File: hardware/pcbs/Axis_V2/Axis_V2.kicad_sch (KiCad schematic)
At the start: 12 parts, among them SW2 RES, U1 ADS1119IPWR, U2 MAX6107, U3 Pico, U5 TCA9534, U9 TCA9548APWR

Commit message: Updates
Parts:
- removed U9: TCA9548APWR, Package_SO:TSSOP-24_4.4x7.8mm_P0.65mm, symbol Interface_Expansion:TCA9548APWR
- added C3: 100n, symbol Device:C_Small
- added J1: Conn_01x12, symbol Connector_Generic:Conn_01x12
- added J12: Conn_01x08, symbol Connector_Generic:Conn_01x08
- added J13: UART, symbol Connector_Generic:Conn_01x03
- added J14: SWD, symbol Connector_Generic:Conn_01x03
- added J4: Conn_01x06, symbol Connector_Generic:Conn_01x06
- added J5: Conn_01x10, Connector_IDC:IDC-Header_2x10_P2.54mm_Vertical, symbol Connector_Generic:Conn_01x10
- added J6: Conn_01x07, symbol Connector_Generic:Conn_01x07
- added J8, J9: Conn_01x03, symbol Connector_Generic:Conn_01x03
- added JP1: EEPROM_WP, Jumper:SolderJumper-3_P2.0mm_Open_TrianglePad1.0x1.5mm, symbol Jumper:SolderJumper_3_Open
- added R15, R16, R17, R18, R19, R20, R21, R22, R23, R24, R25, R26, R3, R4, R5, R6: 1k, symbol Device:R_Small
- added TP1, TP10, TP11, TP12, TP13, TP16, TP17, TP18, TP19, TP4, TP5, TP6, TP7, TP8, TP9: ~, TestPoint:TestPoint_Pad_1.5x1.5mm, symbol Connector:TestPoint
- added U3: FM24CL16B, Package_SO:SOIC-8_3.9x4.9mm_P1.27mm, symbol Memory_NVRAM:FM24CL16B
- added U5: TCA9544A, Package_SO:TSSOP-20_4.4x6.5mm_P0.65mm, symbol Interface_Expansion:TCA9544A
- added U6: 74HC138, symbol 74xx:74HC138
- renumbered C3 to C4, C4 to C5, SW2 to SW1, U5 to U1, U3 to U2, U1 to U4, U2 to U7
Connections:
- net SPI1_CS2 is gone; now on net SPI1_TX: U2.15 (GPIO11)
- net +3V3: now also C3.1, J12.1 (Pin_1), J4.1 (Pin_1), J5.1 (Pin_1), J6.1 (Pin_1), J6.7 (Pin_7), JP1.1 (A), R15.1, R16.1, R17.1, R18.1, R19.1, R20.1, R21.1, R22.1, R23.1, R24.1, R25.1, R26.1, R3.1, R4.1, R5.1, R6.1, U3.8 (VDD), U5.20 (VCC), U6.16 (VCC)
- net +5V: now also J8.1 (Pin_1), J9.1 (Pin_1)
- net 4.5V_VREF: now also TP12.1
- net GND: now also C3.2, J12.8 (Pin_8), J13.2 (Pin_2), J14.2 (Pin_2), J5.2 (Pin_2), J6.2 (Pin_2), J8.3 (Pin_3), J9.3 (Pin_3), JP1.3 (B), U3.4 (VSS), U5.1 (A0), U5.10 (GND), U5.2 (A1), U5.3 (A2), U6.4 (~{E0}), U6.5 (~{E1}), U6.8 (GND); no longer R1.2, U2.32 (GPIO27_ADC1), U4.14 (~{DRDY})
- net I2C0_SCL: now also R1.2, U1.14 (SCL), U2.12 (GPIO9), U5.18 (SCL); no longer U1.15 (SDA), U2.22 (GPIO17)
- net I2C0_SDA: now also R2.2, U1.15 (SDA), U2.11 (GPIO8), U5.19 (SDA); no longer U1.14 (SCL), U2.21 (GPIO16)
- net I2C1_SCL: now also U2.20 (GPIO15), U3.6 (SCL); no longer U2.12 (GPIO9)
- net I2C1_SDA: now also U2.19 (GPIO14), R5.2, R6.2, U3.5 (SDA); no longer U2.14 (GPIO10)
- net SPI0_CS1: now also U2.9 (GPIO6), U6.1 (A0); no longer U2.17 (GPIO13), U2.27 (GPIO21)
- net SPI0_CS2: now also U2.10 (GPIO7), U6.2 (A1); no longer U2.29 (GPIO22)
- net SPI0_RX: now also U2.6 (GPIO4), J5.7 (Pin_7); no longer U2.26 (GPIO20)
- net SPI0_SCK: now also U2.4 (GPIO2), J5.6 (Pin_6); no longer U2.24 (GPIO18)
- net SPI0_TX: now also U2.5 (GPIO3); no longer U2.25 (GPIO19)
- net SPI1_SCK: now also U2.14 (GPIO10), J6.4 (Pin_4); no longer U2.19 (GPIO14)
- net SPI1_TX: now also J6.3 (Pin_3); no longer U2.20 (GPIO15)
- net SWCLK: now also U2.41 (SWCLK), J14.1 (Pin_1)
- net SWDIO: now also U2.43 (SWDIO), J14.3 (Pin_3)
- net UART_RX: now also J13.1 (Pin_1)
- net UART_TX: now also J13.3 (Pin_3)
- net at U2.33 (AGND): now also TP9.1
- net 3WAY: now reaches U2.34 (GPIO28_ADC2)
- net 3WAY: now also J5.5 (Pin_5), TP7.1
- net at U2.35 (ADC_VREF): now also TP8.1
- net SPI0_CS0: now reaches U2.7 (GPIO5)
- net SPI0_CS0: now also U6.6 (E2)
- net ADC_1: now reaches U4.10 (AIN1)
- net ADC_1: now also J9.2 (Pin_2), TP5.1
- net ADC_0: now reaches U4.11 (AIN0)
- net ADC_0: now also J8.2 (Pin_2), TP4.1
- net ADC_3: now reaches U4.6 (AIN3)
- net ADC_3: now also TP11.1
- net ADC_2: now reaches U4.7 (AIN2)
- net ADC_2: now also TP10.1
- net IO_5: now reaches U1.10 (P5)
- net IO_5: now also J1.9 (Pin_9)
- net IO_6: now reaches U1.11 (P6)
- net IO_6: now also J1.10 (Pin_10)
- net IO_7: now reaches U1.12 (P7)
- net IO_7: now also J1.11 (Pin_11)
- net IO_0: now reaches U1.4 (P0)
- net IO_0: now also J1.2 (Pin_2)
- net IO_1: now reaches U1.5 (P1)
- net IO_1: now also J1.3 (Pin_3)
- net IO_2: now reaches U1.6 (P2)
- net IO_2: now also J1.4 (Pin_4)
- net IO_3: now reaches U1.7 (P3)
- net IO_3: now also J1.5 (Pin_5)
- net IO_4: now reaches U1.9 (P4)
- net IO_4: now also J1.8 (Pin_8)
- net SC0 renamed SCL_0
- net SCL_0: now also R15.2, U5.6 (SC0)
- net SD0 renamed SDA_0
- net SDA_0: now also R16.2, U5.5 (SD0)
- net ~{IOEXP_INT} renamed ZC_SIG
- net ZC_SIG: now also J4.2 (Pin_2), J5.3 (Pin_3), TP1.1; no longer U1.13 (~{INT})
- new net 3v3_{IO}: J1.1 (Pin_1), J1.6 (Pin_6)
- new net DISP_DC: J6.6 (Pin_6), U2.29 (GPIO22)
- new net EEPROM_WP: JP1.2 (C), U3.7 (WP)
- new net GND_{IO}: J1.12 (Pin_12), J1.7 (Pin_7)
- new net GPIO_16: J12.2 (Pin_2), U2.21 (GPIO16)
- new net GPIO_17: J12.3 (Pin_3), U2.22 (GPIO17)
- new net GPIO_18: J12.4 (Pin_4), U2.24 (GPIO18)
- new net GPIO_19: J12.5 (Pin_5), U2.25 (GPIO19)
- new net INT_1: R20.2, U5.7 (~{INT1})
- new net INT_2: R23.2, U5.11 (~{INT2})
- new net INT_3: R26.2, TP13.1, U5.14 (~{INT3})
- new net PUMP: J5.4 (Pin_4), TP6.1, U2.32 (GPIO27_ADC1)
- new net SCL_1: R18.2, U5.9 (SC1)
- new net SCL_2: R21.2, U5.13 (SC2)
- new net SCL_3: R24.2, U5.16 (SC3)
- new net SDA_1: R19.2, U5.8 (SD1)
- new net SDA_2: R22.2, U5.12 (SD2)
- new net SDA_3: R25.2, U5.15 (SD3)
- new net SPI0_CS3: U6.3 (A2)
- new net SPI1_CS0: J6.5 (Pin_5), U2.17 (GPIO13)
- new net ~{CS0}: U6.15 (~{Y0})
- new net ~{CS1}: U6.14 (~{Y1})
- new net ~{CS2}: J5.8 (Pin_8), U6.13 (~{Y2})
- new net ~{CS3}: J5.9 (Pin_9), U6.12 (~{Y3})
- new net ~{CS4}: TP16.1, U6.11 (~{Y4})
- new net ~{CS5}: TP17.1, U6.10 (~{Y5})
- new net ~{CS6}: TP18.1, U6.9 (~{Y6})
- new net ~{CS7}: TP19.1, U6.7 (~{Y7})
- new net ~{I2C_IO_INT}: R3.2, R4.2, U1.13 (~{INT}), U2.26 (GPIO20), U2.27 (GPIO21), U5.17 (~{INT})
- new net ~{INT_0}: R17.2, U4.14 (~{DRDY}), U5.4 (~{INT0})
- no-connect marks 4 -> 2
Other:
- removed sheet Peripherals
- note added: "Adding footprints here for resistors in case we'd want to re-use these pins for other purposes. Gives flexibility if a mistake was made during design."
- note added: "Compatible examples: FM24CL16B - fram (C31082) 24C04 - eeprom (C118280) 24C16 - larger eeprom (C79946) etc..."
- note added: "SPI Chip Select, takes a binary signal on A0-2 and converts it to a single pin to be pulled low. If E2 = Low, all outputs are pulled high. Only using 4 SPI peripherals on SPI0 at the moment. SPI1 is dedicated to display."
- note removed: "I2C Expander."
- moved on the sheet: C1, C2, C4, C5, SW1, U1, U2, U4, U7

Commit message: Updates
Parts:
- removed J1: Conn_01x12, symbol Connector_Generic:Conn_01x12
- removed J12: Conn_01x08, symbol Connector_Generic:Conn_01x08
- removed J4: Conn_01x06, symbol Connector_Generic:Conn_01x06
- removed J5: Conn_01x10, Connector_IDC:IDC-Header_2x10_P2.54mm_Vertical, symbol Connector_Generic:Conn_01x10
- removed J6: Conn_01x07, symbol Connector_Generic:Conn_01x07
- removed R15, R16, R17, R18, R19, R20, R21, R22, R23, R24, R25, R26: 1k, symbol Device:R_Small
- removed TP13, TP16, TP17, TP18, TP19: ~, TestPoint:TestPoint_Pad_1.5x1.5mm, symbol Connector:TestPoint
- removed U5: TCA9544A, Package_SO:TSSOP-20_4.4x6.5mm_P0.65mm, symbol Interface_Expansion:TCA9544A
- removed U6: 74HC138, symbol 74xx:74HC138
- added J1: Conn_01x10, symbol Connector_Generic:Conn_01x10
- added J2, J3: Conn_01x02, symbol Connector_Generic:Conn_01x02
- added J4: Conn_01x08, symbol Connector_Generic:Conn_01x08
- added R7, R8, R9: 1k, symbol Device:R_Small
- added U5, U6: MAX31855EASA, Package_SO:SOIC-8_3.9x4.9mm_P1.27mm, symbol Sensor_Temperature:MAX31855EASA
- U2: footprint RPi_Pico:RPi_Pico_SMD_TH -> MCU_RaspberryPi_and_Boards:RPi_Pico_SMD_TH
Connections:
- net IO_0 is gone; now on net IO_1: U1.4 (P0)
- net SCL_0 is gone; now on net I2C0_SCL: U4.16 (SCL)
- net SDA_0 is gone; now on net I2C0_SDA: U4.15 (SDA)
- net +3V3: now also J1.1 (Pin_1), J4.1 (Pin_1), U5.4 (V_CC), U6.4 (V_CC); no longer R4.1, R5.1, R6.1
- net GND: now also J1.2 (Pin_2), J4.8 (Pin_8), U5.1 (GND), U6.1 (GND)
- net I2C1_SDA: no longer R5.2, R6.2
- net IO_1: now also J1.3 (Pin_3); no longer U1.5 (P1)
- net IO_2: now also U1.5 (P1), J1.4 (Pin_4); no longer U1.6 (P2)
- net IO_3: now also U1.6 (P2), J1.5 (Pin_5); no longer U1.7 (P3)
- net IO_4: now also U1.7 (P3), J1.6 (Pin_6); no longer U1.9 (P4)
- net IO_5: now also U1.9 (P4), J1.7 (Pin_7); no longer U1.10 (P5)
- net IO_6: now also U1.10 (P5), J1.8 (Pin_8); no longer U1.11 (P6)
- net IO_7: now also U1.11 (P6), J1.9 (Pin_9); no longer U1.12 (P7)
- net SPI0_CS0: now also U5.6 (~{CS})
- net SPI0_CS1: now also U6.6 (~{CS})
- net SPI0_RX: now also U5.7 (SO), U6.7 (SO)
- net SPI0_SCK: now also U5.5 (SCK), U6.5 (SCK)
- net ~{I2C_IO_INT}: no longer R4.2, U1.13 (~{INT}), U2.26 (GPIO20), U2.27 (GPIO21)
- net 3WAY: no longer names the net of TP7.1, U2.34 (GPIO28_ADC2)
- net DISP_DC: no longer names the net of U2.29 (GPIO22)
- net GPIO_16 renamed HV_IO1
- net HV_IO1: now also R4.1, R4.2, J4.2 (Pin_2)
- net GPIO_17 renamed HV_IO2
- net HV_IO2: now also R5.1, R5.2, J4.3 (Pin_3)
- net GPIO_18 renamed HV_IO3
- net HV_IO3: now also R6.1, R6.2, J4.4 (Pin_4)
- net GPIO_19 renamed HV_IO4
- net HV_IO4: now also J4.5 (Pin_5), R7.1, R7.2
- net PUMP: no longer names the net of TP6.1, U2.32 (GPIO27_ADC1)
- net SPI0_CS2 renamed ~{I2C0_IO_INT}
- net ~{I2C0_IO_INT}: now also U1.13 (~{INT})
- net ZC_SIG: no longer names the net of TP1.1, U2.31 (GPIO26_ADC0)
- new net HV_IO5: J4.6 (Pin_6), R8.1, R8.2, U2.26 (GPIO20)
- new net HV_IO6: J4.7 (Pin_7), R9.1, R9.2, U2.27 (GPIO21)
- new net IO_8: J1.10 (Pin_10), U1.12 (P7)
- new net THCPL1_NEG: J2.2 (Pin_2), U5.2 (T-)
- new net THCPL1_POS: J2.1 (Pin_1), U5.3 (T+)
- new net THCPL2_NEG: J3.2 (Pin_2), U6.2 (T-)
- new net THCPL2_POS: J3.1 (Pin_1), U6.3 (T+)
- no-connect marks 2 -> 3
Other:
- note added: "GPIO expander. Switches, buttons, etc. can be wired here and used as input/output. No signals such as I2C."
- note removed: "Adding footprints here for resistors in case we'd want to re-use these pins for other purposes. Gives flexibility if a mistake was made during design."
- note removed: "GPIO expander. Switches, buttons, etc. can be wired here and used an input/output. No signals such as I2C."
- note removed: "SPI Chip Select, takes a binary signal on A0-2 and converts it to a single pin to be pulled low. If E2 = Low, all outputs are pulled high. Only using 4 SPI peripherals on SPI0 at the moment. SPI1 is dedicated to display."
- moved on the sheet: C1, C2, C3, C4, C5, J13, J14, J8, J9, JP1, R1, R2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

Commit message: PCB Updates
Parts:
- removed J8, J9: Conn_01x03, symbol Connector_Generic:Conn_01x03
- removed JP1: EEPROM_WP, Jumper:SolderJumper-3_P2.0mm_Open_TrianglePad1.0x1.5mm, symbol Jumper:SolderJumper_3_Open
- removed TP1, TP10, TP11, TP12, TP4, TP5, TP6, TP7, TP8, TP9: ~, TestPoint:TestPoint_Pad_1.5x1.5mm, symbol Connector:TestPoint
- added J5: Conn_01x04, TerminalBlock_Phoenix:TerminalBlock_Phoenix_MKDS-1,5-4-5.08_1x04_P5.08mm_Horizontal, symbol Connector_Generic:Conn_01x04
- C1: renamed from C4; footprint (none) -> Capacitor_SMD:C_0402_1005Metric_Pad0.74x0.62mm_HandSolder
- C2: renamed from C3; value 100n -> 0.1u; footprint (none) -> Capacitor_SMD:C_0402_1005Metric_Pad0.74x0.62mm_HandSolder
- C3: renamed from C5; footprint (none) -> Capacitor_SMD:C_0402_1005Metric_Pad0.74x0.62mm_HandSolder
- C4: renamed from C1; footprint (none) -> Capacitor_SMD:C_0402_1005Metric_Pad0.74x0.62mm_HandSolder
- C5: renamed from C2; footprint (none) -> Capacitor_SMD:C_0402_1005Metric_Pad0.74x0.62mm_HandSolder
- J1: renamed from J14; footprint (none) -> Connector_JST:JST_SH_BM03B-SRSS-TB_1x03-1MP_P1.00mm_Vertical
- J2: renamed from J13; footprint (none) -> Connector_JST:JST_SH_BM03B-SRSS-TB_1x03-1MP_P1.00mm_Vertical
- J3: renamed from J2; footprint (none) -> TerminalBlock_Phoenix:TerminalBlock_Phoenix_MKDS-1,5-2-5.08_1x02_P5.08mm_Horizontal
- J4: renamed from J3; footprint (none) -> TerminalBlock_Phoenix:TerminalBlock_Phoenix_MKDS-1,5-2-5.08_1x02_P5.08mm_Horizontal
- J6: renamed from J1; footprint (none) -> TerminalBlock_RND:TerminalBlock_RND_205-00240_1x10_P5.08mm_Horizontal
- J7: renamed from J4; footprint (none) -> Connector_IDC:IDC-Header_2x04_P2.54mm_Vertical
- R1, R2, R3, R4, R5, R6, R7, R8, R9: footprint (none) -> Resistor_SMD:R_0402_1005Metric_Pad0.72x0.64mm_HandSolder
- U7: renamed from U1; footprint (none) -> Package_SO:SOIC-16W_7.5x10.3mm_P1.27mm
- renumbered U2 to U1, U5 to U2, U6 to U3, U7 to U4, U3 to U5, U4 to U6
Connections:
- net EEPROM_WP is gone; now on net GND: U5.7 (WP)
- net ~{I2C_IO_INT} is gone; now on net ~{I2C0_IO_INT}: R3.2
- net ~{INT_0} is gone; now on net ~{I2C0_ADS_RDY}: U6.14 (~{DRDY})
- net +5V: now also J5.1 (Pin_1)
- net ADC_0: now also J5.3 (Pin_3)
- net ADC_1: now also J5.4 (Pin_4)
- net GND: now also J5.2 (Pin_2)
- net ~{I2C0_ADS_RDY}: now reaches U1.29 (GPIO22)
- no-connect marks 3 -> 14
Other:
- moved on the sheet: R1, R2, R3

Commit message: Updates
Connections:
- net HV_IO1: no longer J7.2 (Pin_2), R4.1
- net HV_IO2: no longer J7.3 (Pin_3), R5.1
- net HV_IO3: no longer J7.4 (Pin_4), R6.1
- net HV_IO4: no longer J7.5 (Pin_5), R7.1
- net HV_IO5: no longer J7.6 (Pin_6), R8.1
- net HV_IO6: no longer J7.7 (Pin_7), R9.1
- net SPI0_TX: no longer U1.5 (GPIO3)
- net SPI1_CS0: no longer U1.17 (GPIO13)
- net SPI1_RX: no longer U1.16 (GPIO12)
- net SPI1_SCK: no longer U1.14 (GPIO10)
- net SPI1_TX: no longer U1.15 (GPIO11)
- new net: J7.4 (Pin_4), R6.1
- new net: J7.6 (Pin_6), R8.1
- new net: J7.3 (Pin_3), R5.1
- new net: J7.2 (Pin_2), R4.1
- new net: J7.7 (Pin_7), R9.1
- new net: J7.5 (Pin_5), R7.1

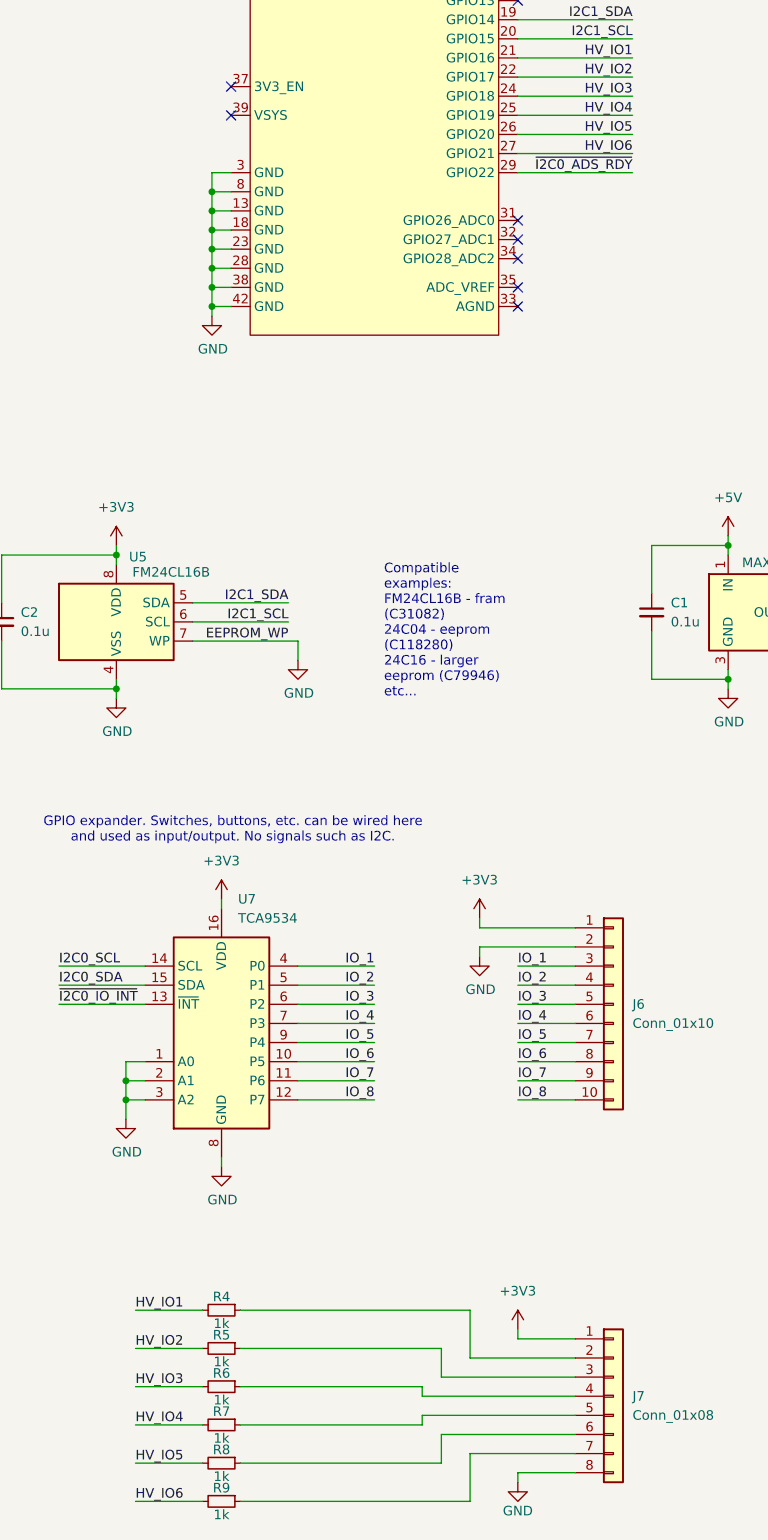
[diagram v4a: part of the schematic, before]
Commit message: Updates to V2 pcb, add HV pcb
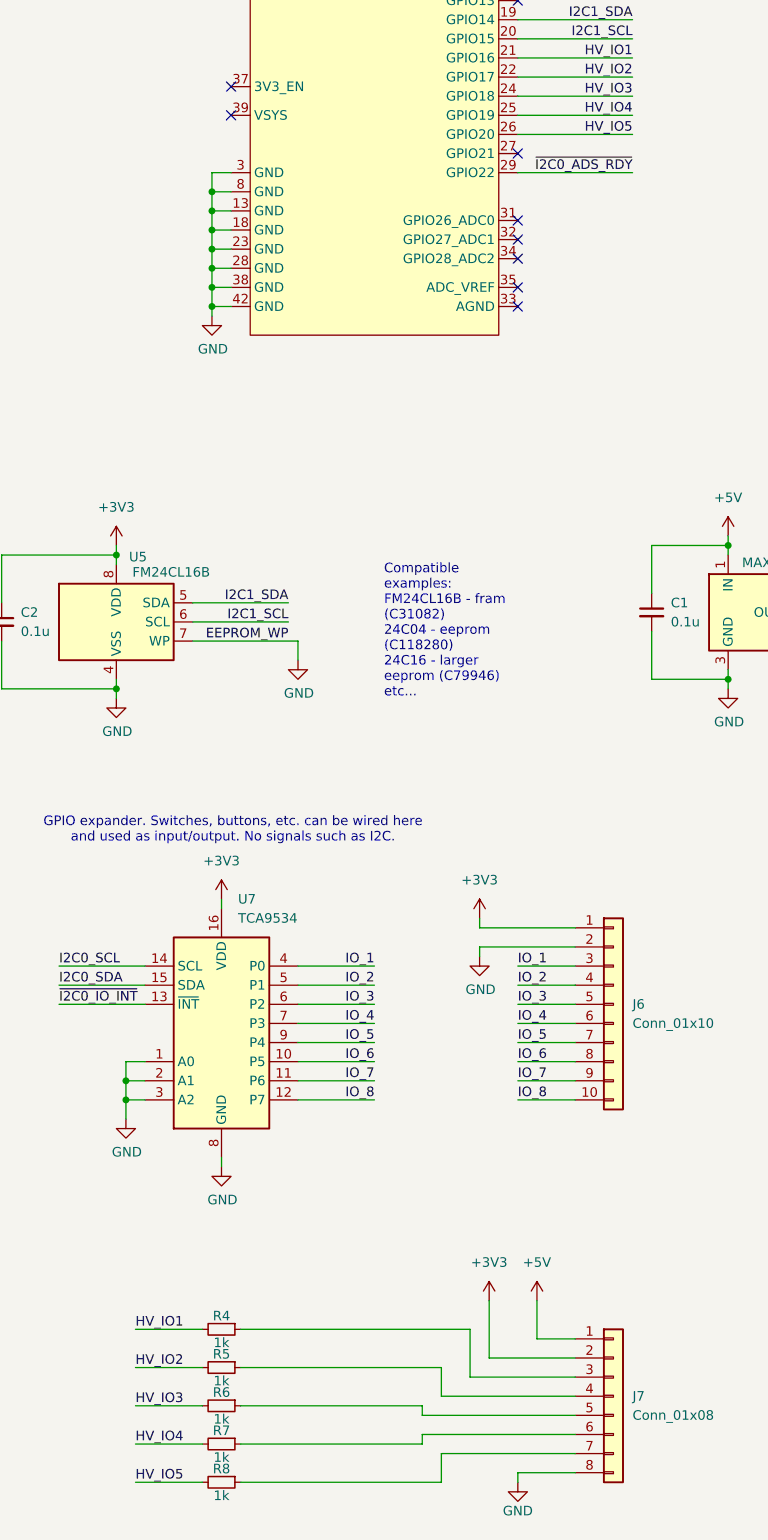
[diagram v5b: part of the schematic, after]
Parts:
- removed R9: 1k, Resistor_SMD:R_0402_1005Metric_Pad0.72x0.64mm_HandSolder, symbol Device:R_Small
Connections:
- net +3V3: now also J7.2 (Pin_2); no longer J7.1 (Pin_1)
- net +5V: now also J7.1 (Pin_1)
- net at R6.1: now also J7.5 (Pin_5); no longer J7.4 (Pin_4)
- net at J7.6 (Pin_6): now also R7.1; no longer R8.1
- net at J7.3 (Pin_3): now also R4.1; no longer R5.1
- net at J7.7 (Pin_7): now also R8.1
- net HV_IO6: no longer names the net of U1.27 (GPIO21)
- new net: J7.4 (Pin_4), R5.1
- no-connect marks 14 -> 15

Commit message: More changes, wow! Who would have thought?
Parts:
- added BT1: BA2032, symbol Device:Battery_Cell
- added C6: 0.1u, Capacitor_SMD:C_0402_1005Metric_Pad0.74x0.62mm_HandSolder, symbol Device:C_Small
- added U9: DS3231MZ, Package_SO:SOIC-8_3.9x4.9mm_P1.27mm, symbol Timer_RTC:DS3231MZ
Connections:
- net +3V3: now also C6.1, U9.2 (VCC)
- net GND: now also BT1.2 (-), C6.2, U9.5 (GND)
- net I2C0_SCL: now also U9.8 (SCL)
- net I2C0_SDA: now also U9.7 (SDA)
- net ~{TIMER_INT}: now reaches U1.27 (GPIO21)
- net ~{TIMER_INT}: now also U9.3 (~{INT}/SQW)
- net ~{I2C0_IO_INT} renamed ~{I2C0_IO_INT_B}
- new net +BATT: BT1.1 (+), U9.6 (VBAT)
- no-connect marks 15 -> 16

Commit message: More updates and changes
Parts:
- added R10, R9: 1k, Resistor_SMD:R_0402_1005Metric_Pad0.72x0.64mm_HandSolder, symbol Device:R_Small
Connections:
- net +3V3: now also R10.1, R9.1
- net HV_IO1: now also U1.20 (GPIO15); no longer U1.21 (GPIO16)
- net HV_IO2: now also U1.21 (GPIO16); no longer U1.22 (GPIO17)
- net HV_IO3: now also U1.22 (GPIO17); no longer U1.24 (GPIO18)
- net HV_IO4: now also U1.24 (GPIO18); no longer U1.25 (GPIO19)
- net HV_IO5: now also U1.25 (GPIO19); no longer U1.26 (GPIO20)
- net I2C0_SCL: now also R9.2; no longer R1.2, U6.16 (SCL), U7.14 (SCL), U9.8 (SCL)
- net I2C0_SDA: now also R10.2; no longer R2.2, U6.15 (SDA), U7.15 (SDA), U9.7 (SDA)
- net I2C1_SCL: now also R1.2, U1.27 (GPIO21), U6.16 (SCL), U7.14 (SCL), U9.8 (SCL); no longer U1.20 (GPIO15)
- net I2C1_SDA: now also R2.2, U1.26 (GPIO20), U6.15 (SDA), U7.15 (SDA), U9.7 (SDA); no longer U1.19 (GPIO14)
- net SPI0_CS0: no longer U2.6 (~{CS})
- net SPI0_CS1: no longer U3.6 (~{CS})
- net SPI0_RX: no longer U2.7 (SO), U3.7 (SO)
- net SPI0_SCK: no longer U2.5 (SCK), U3.5 (SCK)
- net SPI0_TX: now also U1.5 (GPIO3)
- net SPI1_CS0: now also U1.19 (GPIO14), U2.6 (~{CS})
- net SPI1_RX: now also U1.17 (GPIO13), U2.7 (SO), U3.7 (SO)
- net SPI1_SCK: now also U1.15 (GPIO11), U2.5 (SCK), U3.5 (SCK)
- net SPI1_TX: now also U1.16 (GPIO12)
- net ~{TIMER_INT}: now also U1.31 (GPIO26_ADC0); no longer U1.27 (GPIO21)
- net SPI1_CS1: now reaches U1.14 (GPIO10)
- net SPI1_CS1: now also U3.6 (~{CS})
- net ~{I2C1_IO_INT_B}: now reaches U1.32 (GPIO27_ADC1)
- net ~{I2C1_IO_INT_B}: now also R3.2, U7.13 (~{INT})
- net ~{I2C1_ADS_RDY}: now reaches U1.34 (GPIO28_ADC2)
- net ~{I2C1_ADS_RDY}: now also U6.14 (~{DRDY})
- net ~{I2C0_ADS_RDY}: no longer names the net of U1.29 (GPIO22)
- net ~{I2C0_ADS_RDY}: no longer U6.14 (~{DRDY})
- removed net ~{I2C0_IO_INT_B}: R3.2, U1.10 (GPIO7), U7.13 (~{INT})
- no-connect marks 16 -> 8
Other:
- moved on the sheet: BT1, C6, R4, R5, R6, R7, R8
